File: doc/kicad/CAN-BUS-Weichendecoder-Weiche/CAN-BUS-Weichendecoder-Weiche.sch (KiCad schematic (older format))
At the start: 43 parts, among them J1 250-1404, J2 250-1404, J22 CAN-BUS, J23 CAN-BUS, J3 250-1404, J4 250-1404, J5 250-1404, J6 GND 12V DC +, J7 DCC IN, J8 I²C D C + -, U1 6N136, U2 Arduino_Nano, U3 ULN2803A, U4 ULN2803A, U5 TSR_1-2450

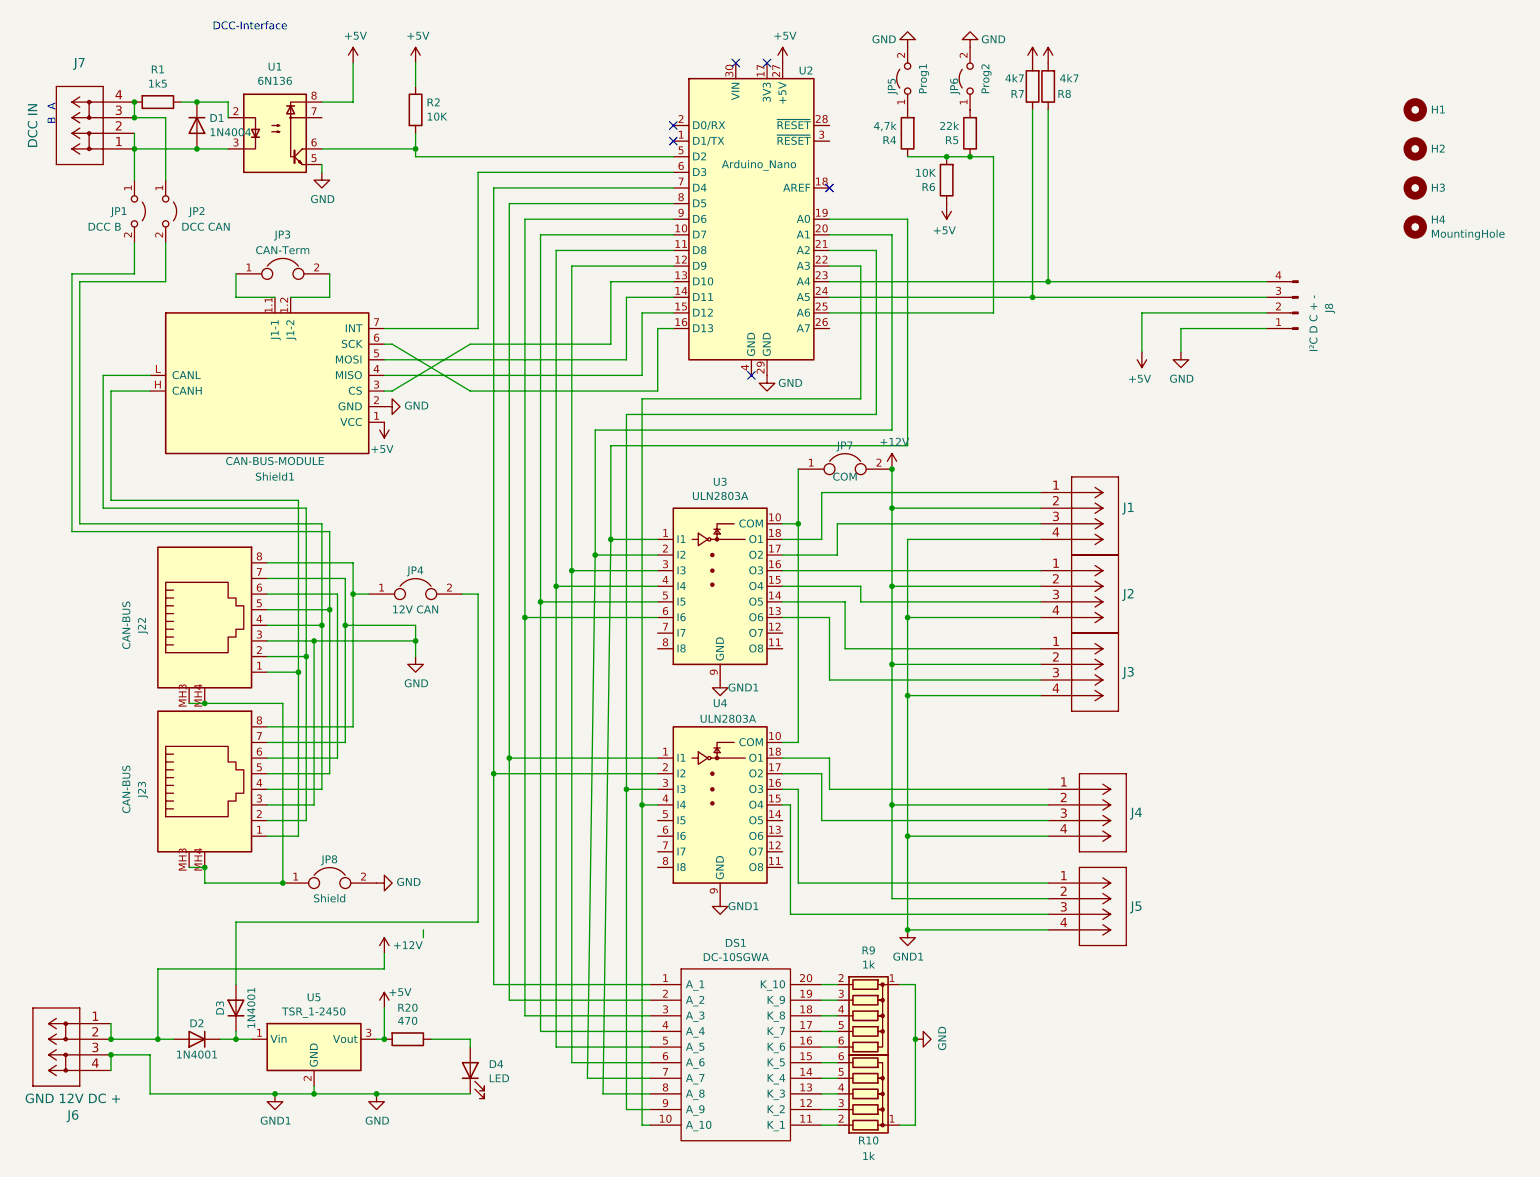
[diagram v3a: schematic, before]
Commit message: Buchen zu den Weichen gedreht, damit sie besser auf das Board passsen
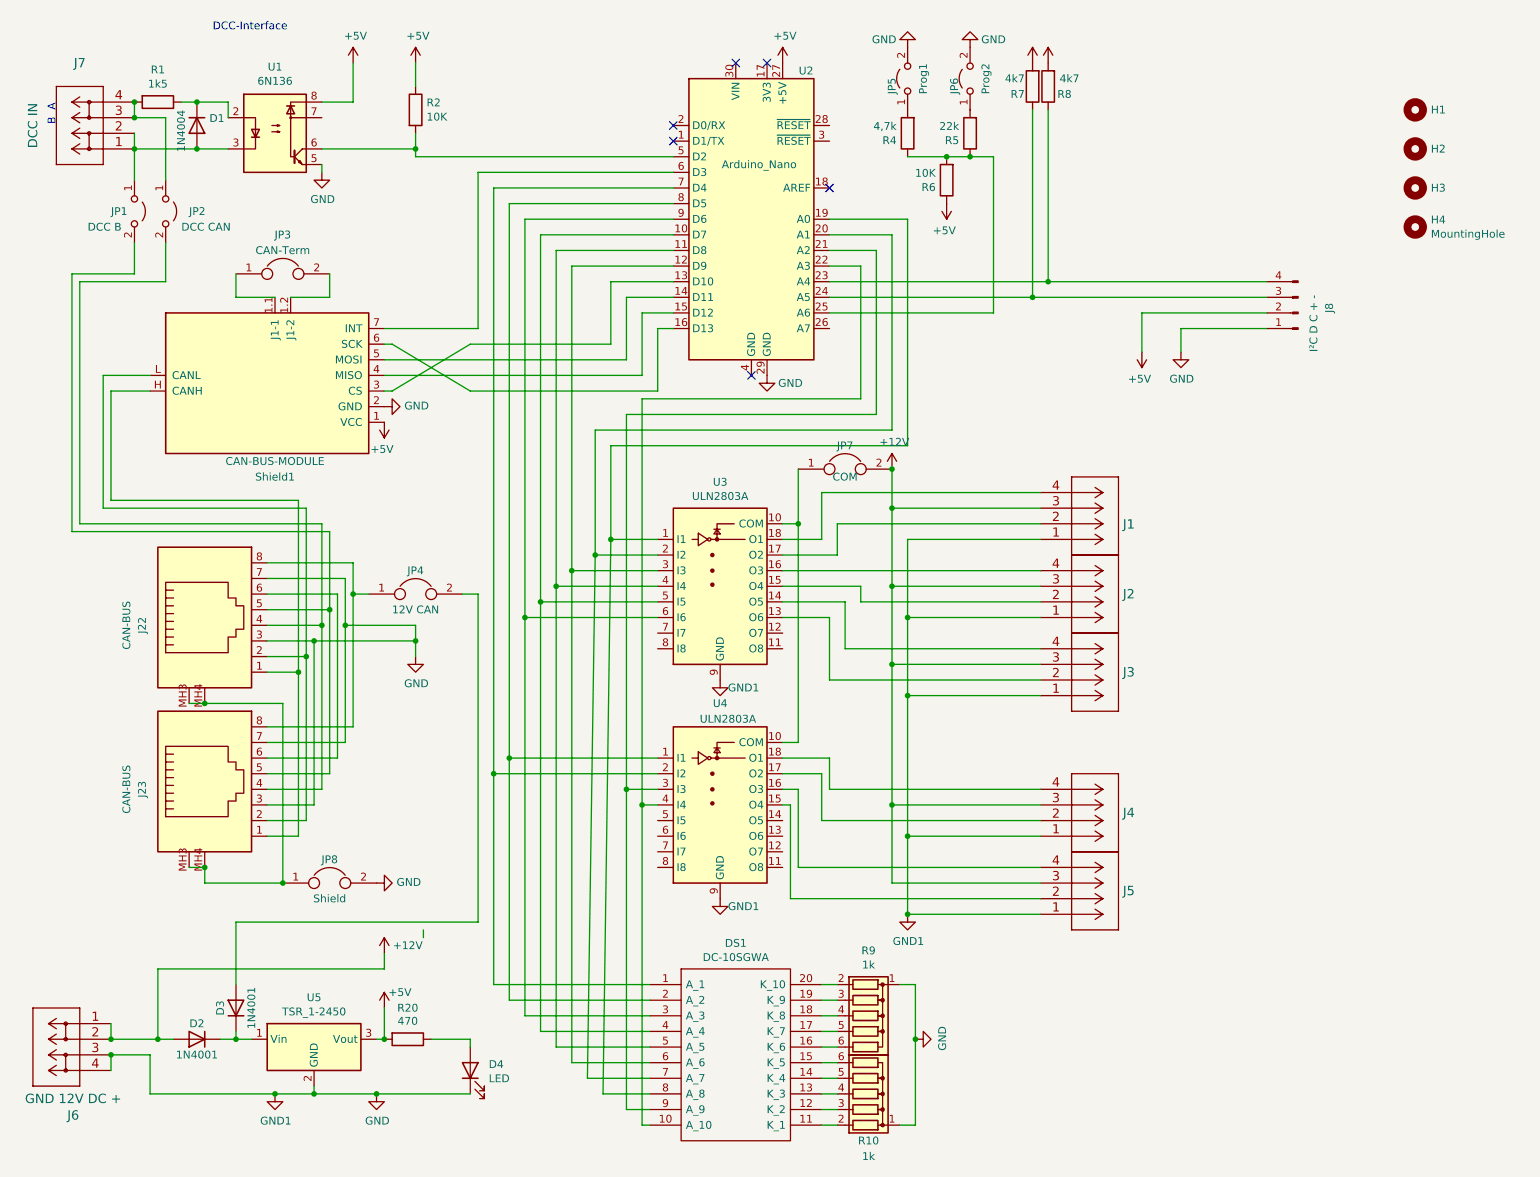
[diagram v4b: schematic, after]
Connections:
- net +12V: now also J1.3, J2.3, J3.3, J4.3, J5.3; no longer J1.2, J2.2, J3.2, J4.2, J5.2
- net GND: now also J1.1, J2.1, J3.1, J4.1, J5.1; no longer J1.4, J2.4, J3.4, J4.4, J5.4
- net at U3.13 (O6): now also J3.2; no longer J3.3
- net at U3.14 (O5): now also J3.4; no longer J3.1
- net at U3.15 (O4): now also J2.2; no longer J2.3
- net at U3.16 (O3): now also J2.4; no longer J2.1
- net at U3.17 (O2): now also J1.2; no longer J1.3
- net at U3.18 (O1): now also J1.4; no longer J1.1
- net at U4.15 (O4): now also J5.2; no longer J5.3
- net at U4.16 (O3): now also J5.4; no longer J5.1
- net at U4.17 (O2): now also J4.2; no longer J4.3
- net at U4.18 (O1): now also J4.4; no longer J4.1
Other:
- moved on the sheet: J4, J5
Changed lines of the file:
@@
 P 1700 1150
 F 0 "D1" V 1654 1230 50  0000 L CNN
-F 1 "1N4004" V 1745 1230 50  0000 L CNN
+F 1 "1N4004" H 1600 1050 50  0000 L CNN
 F 2 "Diodes_THT:D_DO-15_P10.16mm_Horizontal" H 1700 975 50  0001 C CNN
 F 3 "http://www.vishay.com/docs/88503/1n4001.pdf" H 1700 1150 50  0001 C CNN
@@
 L Wago:250-1404 J5
 U 1 1 616E29D2
-P 7150 6000
-F 0 "J5" H 7678 5850 60  0000 L CNN
-F 1 "250-1404" H 7678 5850 60  0001 L CNN
-F 2 "Wago:CONN_250-1404_WAG" H 7678 5744 60  0001 L CNN
-F 3 "" H 7150 6000 60  0001 C CNN
-	1    7150 6000
-	1    0    0    -1
-$EndComp
-Wire Wire Line
-	7150 6300 6250 6300
+P 7100 6200
+F 0 "J5" H 7628 6050 60  0000 L CNN
+F 1 "250-1404" H 7628 6050 60  0001 L CNN
+F 2 "Wago:CONN_250-1404_WAG" H 7628 5944 60  0001 L CNN
+F 3 "" H 7100 6200 60  0001 C CNN
+	1    7100 6200
+	1    0    0    1
+$EndComp
+Wire Wire Line
+	7100 6200 6250 6200
 Wire Wire Line
 	4450 7450 4600 7450
@@
 	6250 4300 6250 4800
 Wire Wire Line
-	7150 5700 6250 5700
+	7100 5700 6250 5700
 $Comp
 L Wago:250-1404 J4
 U 1 1 616E1E7E
-P 7150 5400
-F 0 "J4" H 7678 5250 60  0000 L CNN
-F 1 "250-1404" H 7678 5250 60  0001 L CNN
-F 2 "Wago:CONN_250-1404_WAG" H 7678 5144 60  0001 L CNN
-F 3 "" H 7150 5400 60  0001 C CNN
-	1    7150 5400
-	1    0    0    -1
+P 7100 5700
+F 0 "J4" H 7628 5550 60  0000 L CNN
+F 1 "250-1404" H 7628 5550 60  0001 L CNN
+F 2 "Wago:CONN_250-1404_WAG" H 7628 5444 60  0001 L CNN
+F 3 "" H 7100 5700 60  0001 C CNN
+	1    7100 5700
+	1    0    0    1
 $EndComp
 Wire Wire Line
@@
 L Wago:250-1404 J3
 U 1 1 616E033D
-P 7100 4500
-F 0 "J3" H 7628 4350 60  0000 L CNN
-F 1 "250-1404" H 7628 4350 60  0001 L CNN
-F 2 "Wago:CONN_250-1404_WAG" H 7628 4244 60  0001 L CNN
-F 3 "" H 7100 4500 60  0001 C CNN
-	1    7100 4500
-	1    0    0    -1
+P 7100 4800
+F 0 "J3" H 7628 4650 60  0000 L CNN
+F 1 "250-1404" H 7628 4650 60  0001 L CNN
+F 2 "Wago:CONN_250-1404_WAG" H 7628 4544 60  0001 L CNN
+F 3 "" H 7100 4800 60  0001 C CNN
+	1    7100 4800
+	1    0    0    1
 $EndComp
 Wire Wire Line
@@
 L Wago:250-1404 J2
 U 1 1 616186ED
-P 7100 4000
-F 0 "J2" H 7628 3850 60  0000 L CNN
-F 1 "250-1404" H 7628 3850 60  0001 L CNN
-F 2 "Wago:CONN_250-1404_WAG" H 7628 3744 60  0001 L CNN
-F 3 "" H 7100 4000 60  0001 C CNN
-	1    7100 4000
-	1    0    0    -1
+P 7100 4300
+F 0 "J2" H 7628 4150 60  0000 L CNN
+F 1 "250-1404" H 7628 4150 60  0001 L CNN
+F 2 "Wago:CONN_250-1404_WAG" H 7628 4044 60  0001 L CNN
+F 3 "" H 7100 4300 60  0001 C CNN
+	1    7100 4300
+	1    0    0    1
 $EndComp
 Wire Wire Line
@@
 L power:GND1 #PWR0104
 U 1 1 61C3B5F7
-P 6250 6300
-F 0 "#PWR0104" H 6250 6050 50  0001 C CNN
-F 1 "GND1" H 6255 6127 50  0000 C CNN
-F 2 "" H 6250 6300 50  0001 C CNN
-F 3 "" H 6250 6300 50  0001 C CNN
-	1    6250 6300
-	1    0    0    -1
-$EndComp
-Connection ~ 6250 6300
+P 6250 6200
+F 0 "#PWR0104" H 6250 5950 50  0001 C CNN
+F 1 "GND1" H 6255 6027 50  0000 C CNN
+F 2 "" H 6250 6200 50  0001 C CNN
+F 3 "" H 6250 6200 50  0001 C CNN
+	1    6250 6200
+	1    0    0    -1
+$EndComp
+Connection ~ 6250 6200
 $Comp
 L power:GND1 #PWR0105
@@
 	7150 2150 8550 2150
 Wire Wire Line
-	5500 5500 5500 6200
-Wire Wire Line
-	5550 5400 5550 6000
+	5550 5400 5550 5900
 Wire Wire Line
 	7100 4300 6250 4300
@@
 Connection ~ 6150 4600
 Wire Wire Line
-	7150 5500 6150 5500
+	7100 5500 6150 5500
 Connection ~ 6150 5500
 Wire Wire Line
-	6250 5700 6250 6300
-Wire Wire Line
-	7150 6100 6150 6100
-Wire Wire Line
-	6150 5500 6150 6100
+	6250 5700 6250 6200
+Wire Wire Line
+	6150 5500 6150 6000
 Wire Wire Line
 	6250 4800 6250 5700
@@
 	6150 4600 6150 5500
 Wire Wire Line
-	5700 5600 7150 5600
-Wire Wire Line
-	5500 6200 7150 6200
-Wire Wire Line
-	5750 5400 7150 5400
-Wire Wire Line
-	5550 6000 7150 6000
+	5700 5600 7100 5600
+Wire Wire Line
+	5750 5400 7100 5400
 Wire Wire Line
 	4550 2900 4550 5500
@@
 L Wago:250-1404 J1
 U 1 1 62056259
-P 7100 3500
-F 0 "J1" H 7628 3403 60  0000 L CNN
-F 1 "250-1404" H 7628 3297 60  0001 L CNN
-F 2 "Wago:CONN_250-1404_WAG" H 7500 3240 60  0001 C CNN
-F 3 "" H 7100 3500 60  0001 C CNN
-	1    7100 3500
-	1    0    0    -1
+P 7100 3800
+F 0 "J1" H 7628 3703 60  0000 L CNN
+F 1 "250-1404" H 7628 3597 60  0001 L CNN
+F 2 "Wago:CONN_250-1404_WAG" H 7500 3540 60  0001 C CNN
+F 3 "" H 7100 3800 60  0001 C CNN
+	1    7100 3800
+	1    0    0    1
 $EndComp
 Wire Wire Line
@@
 Wire Wire Line
 	2550 3750 900  3750
+Wire Wire Line
+	5550 5900 7100 5900
+Wire Wire Line
+	7100 6000 6150 6000
+Wire Wire Line
+	5500 6100 7100 6100
+Wire Wire Line
+	5500 5500 5500 6100
 $EndSCHEMATC

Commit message: Aufgeräumt
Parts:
- added C1: 22µ/16V, Capacitors_THT:CP_Radial_D4.0mm_P1.50mm, symbol Device:CP
- DS1: Preis (none) -> 2,10; Quelle (none) -> https://www.reichelt.de/bargraph-anzeige-10-elemente-gruen-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
- J1, J2, J3, J4, J5: Preis (none) -> 0,71; Quelle (none) -> https://www.voelkner.de/products/55695/WAGO-250-1404-Federk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
- J22, J23: Preis (none) -> 0,70; Quelle (none) -> https://www.reichelt.de/modular-einbaubuchse-8-8-geschirmt-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
- R10, R9: Preis (none) -> 0,07; Quelle (none) -> https://www.reichelt.de/widerstandsnetzwerk-1-0-kohm-sterns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
- Shield1: Preis (none) -> 2,90; Quelle (none) -> https://www.marotronics.de/MCP2515-Can-Bus-Modul-mit-TJA105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
- U1: Preis (none) -> 0,52; Quelle (none) -> https://www.reichelt.de/optokoppler-6n-137-p2858.html
- U2: Preis (none) -> 5,85; Quelle (none) -> https://www.makershop.de/plattformen/arduino/3-nano-v3/
- U3, U4: Preis (none) -> 0,41; Quelle (none) -> https://www.reichelt.de/eight-darlington-arrays-dil-18-uln-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
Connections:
- net +5V: now also C1.1
- net GND: now also C1.2
- net at DS1.4 (A_4), U2.10 (D7): now also U4.1 (I1); no longer U3.5 (I5)
- net at DS1.5 (A_5), U2.11 (D8): now also U3.6 (I6); no longer U3.4 (I4)
- net at DS1.6 (A_6), U2.12 (D9): now also U3.5 (I5); no longer U3.3 (I3)
- net at DS1.8 (A_8), U2.19 (A0): now also U3.3 (I3); no longer U3.1 (I1)
- net at DS1.7 (A_7), U2.20 (A1): now also U3.4 (I4); no longer U3.2 (I2)
- net at DS1.9 (A_9), U2.21 (A2): now also U3.2 (I2); no longer U4.3 (I3)
- net at DS1.10 (A_10), U2.22 (A3): now also U3.1 (I1); no longer U4.4 (I4)
- net at DS1.1 (A_1), U2.7 (D4): now also U4.4 (I4); no longer U4.2 (I2)
- net at DS1.2 (A_2), U2.8 (D5): now also U4.3 (I3); no longer U4.1 (I1)
- net at DS1.3 (A_3), U2.9 (D6): now also U4.2 (I2); no longer U3.6 (I6)
- no-connect marks 6 -> 18
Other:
- moved on the sheet: R1, R20
